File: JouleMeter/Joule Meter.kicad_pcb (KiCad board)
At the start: 4 copper layers, 153.8 x 95 mm, 82 parts, among them J1 XT60-M, J2 XT60-M, J3 22035035, J4 22035035, J5 M22-7130442, U1 LMR36510, U3 INA240A1PW, U4 ADS1118IDGS-Q1, U5 MCP6286T-E/OT1, U6 MCP2562

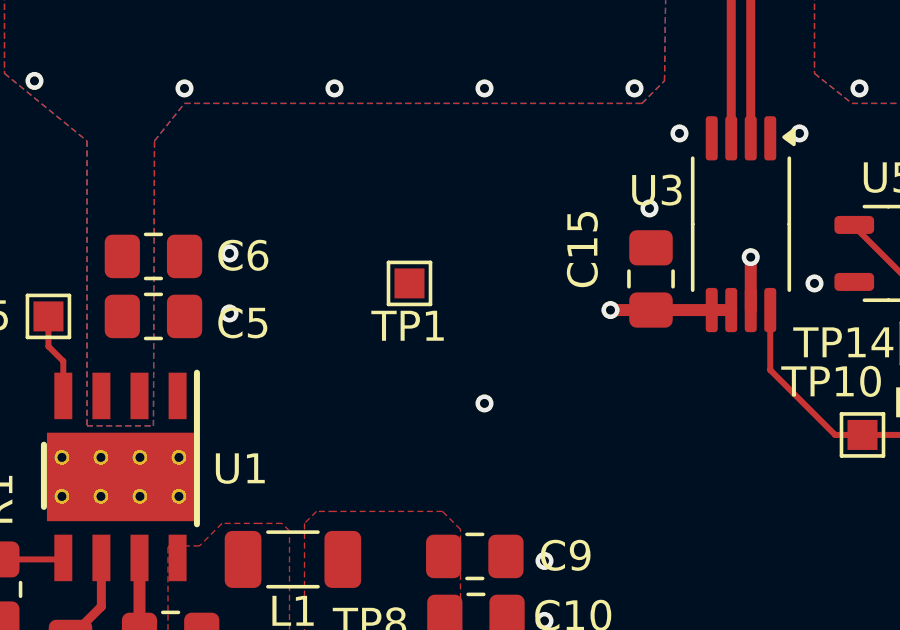
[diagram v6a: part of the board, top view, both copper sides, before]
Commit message: Joule Meter Final
Added a second test pad for the ground. The idea is that we can connect a wire across these two to make a test loop.
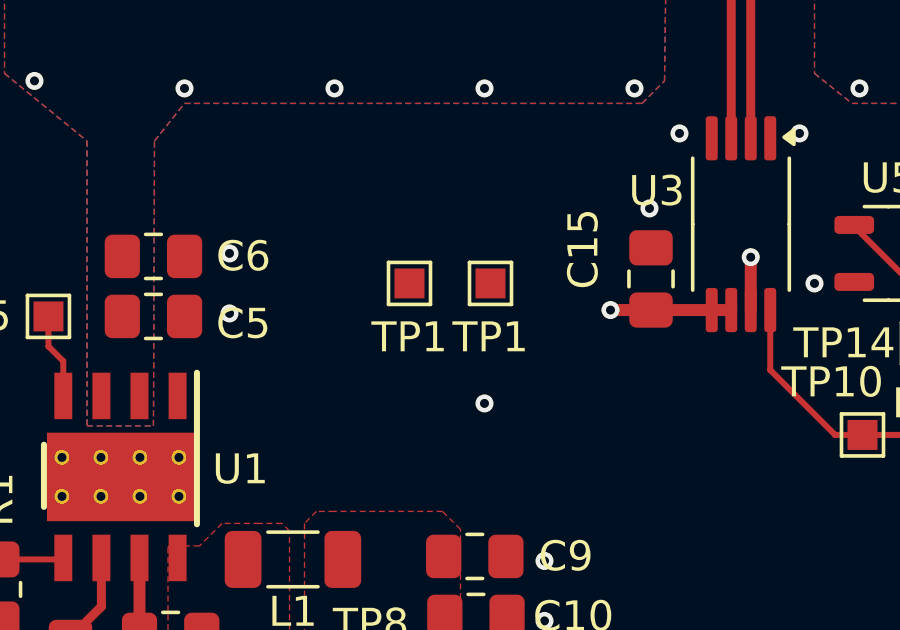
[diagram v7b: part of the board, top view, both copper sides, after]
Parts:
- added TP1: Ground, TestPoint:TestPoint_Pad_1.0x1.0mm, F.Cu at (90.2, 66.0)
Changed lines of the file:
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@@
 		(tags "test point SMD pad rectangle square")
 		(property "Reference" "TP1"
-			(at 0 -1.448 0)
+			(at 0 -1.8 0)
 			(layer "F.SilkS")
 			(effects
@@
 		)
 	)
+	(footprint "TestPoint:TestPoint_Pad_1.0x1.0mm"
+		(layer "F.Cu")
+		(at 90.2 66 180)
+		(descr "SMD rectangular pad as test Point, square 1.0mm side length")
+		(tags "test point SMD pad rectangle square")
+		(property "Reference" "TP1"
+			(at 0 -1.8 0)
+			(layer "F.SilkS")
+			(effects
+				(font
+					(size 1 1)
+					(thickness 0.15)
+				)
+			)
+		)
+		(property "Value" "Ground"
+			(at 0 1.55 0)
+			(layer "F.Fab")
+			(hide yes)
+			(effects
+				(font
+					(size 1 1)
+					(thickness 0.15)
+				)
+			)
+		)
+		(property "Datasheet" ""
+			(at 0 0 180)
+			(unlocked yes)
+			(layer "F.Fab")
+			(hide yes)
+			(effects
+				(font
+					(size 1.27 1.27)
+					(thickness 0.15)
+				)
+			)
+		)
+		(property "Description" "test point"
+			(at 0 0 180)
+			(unlocked yes)
+			(layer "F.Fab")
+			(hide yes)
+			(effects
+				(font
+					(size 1.27 1.27)
+					(thickness 0.15)
+				)
+			)
+		)
+		(attr exclude_from_pos_files)
+		(fp_line
+			(start 0.7 0.7)
+			(end -0.7 0.7)
+			(stroke
+				(width 0.12)
+				(type solid)
+			)
+			(layer "F.SilkS")
+		)
+		(fp_line
+			(start 0.7 -0.7)
+			(end 0.7 0.7)
+			(stroke
+				(width 0.12)
+				(type solid)
+			)
+			(layer "F.SilkS")
+		)
+		(fp_line
+			(start -0.7 0.7)
+			(end -0.7 -0.7)
+			(stroke
+				(width 0.12)
+				(type solid)
+			)
+			(layer "F.SilkS")
+		)
+		(fp_line
+			(start -0.7 -0.7)
+			(end 0.7 -0.7)
+			(stroke
+				(width 0.12)
+				(type solid)
+			)
+			(layer "F.SilkS")
+		)
+		(fp_line
+			(start 1 1)
+			(end 1 -1)
+			(stroke
+				(width 0.05)
+				(type solid)
+			)
+			(layer "F.CrtYd")
+		)
+		(fp_line
+			(start 1 1)
+			(end -1 1)
+			(stroke
+				(width 0.05)
+				(type solid)
+			)
+			(layer "F.CrtYd")
+		)
+		(fp_line
+			(start -1 -1)
+			(end 1 -1)
+			(stroke
+				(width 0.05)
+				(type solid)
+			)
+			(layer "F.CrtYd")
+		)
+		(fp_line
+			(start -1 -1)
+			(end -1 1)
+			(stroke
+				(width 0.05)
+				(type solid)
+			)
+			(layer "F.CrtYd")
+		)
+		(fp_text user "${REFERENCE}"
+			(at 0.05 1.7875 0)
+			(layer "F.Fab")
+			(effects
+				(font
+					(size 1 1)
+					(thickness 0.15)
+				)
+			)
+		)
+		(pad "1" smd rect
+			(at 0 0 180)
+			(size 1 1)
+			(layers "F.Cu" "F.Mask")
+			(net 1 "GND")
+			(pinfunction "1")
+			(pintype "passive")
+		)
+		(embedded_fonts no)
+	)
 	(footprint "Resistor_SMD:R_0805_2012Metric"

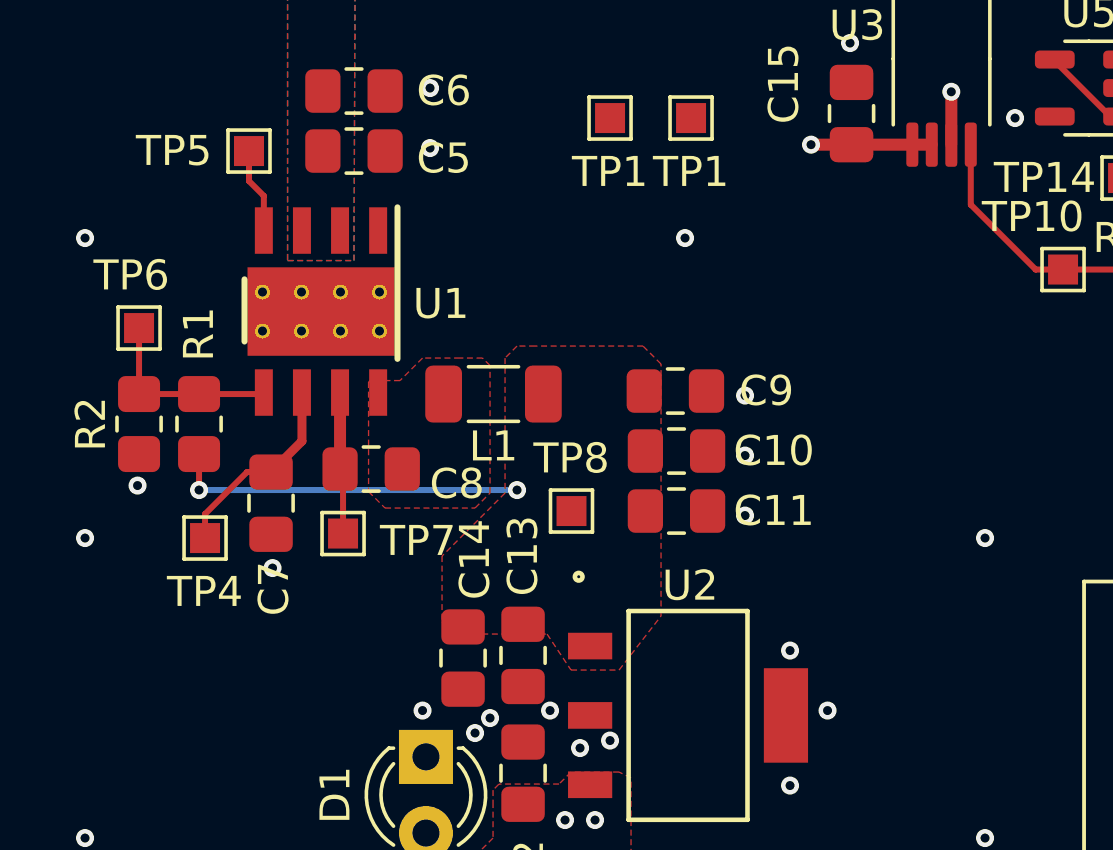
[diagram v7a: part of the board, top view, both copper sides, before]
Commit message: changed the inductor footprint
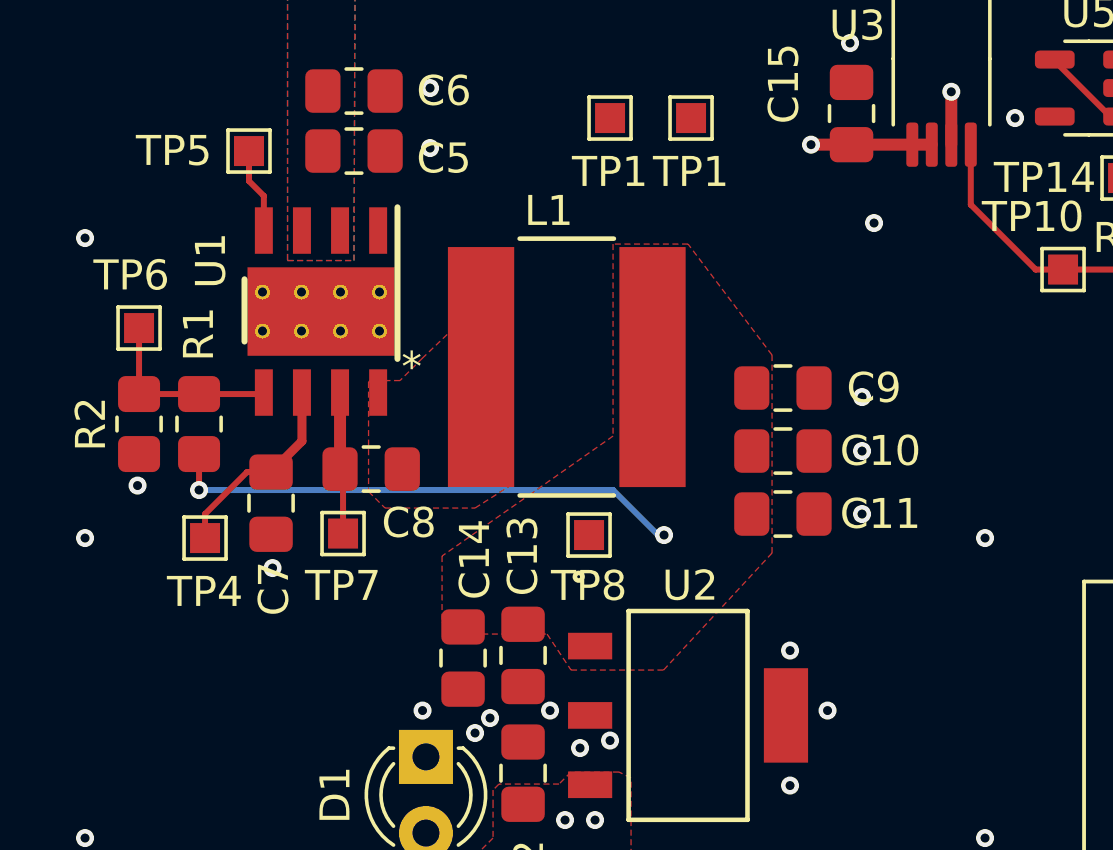
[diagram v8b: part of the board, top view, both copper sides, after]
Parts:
- L1: footprint Inductor_SMD:L_1206_3216Metric_Pad1.22x1.90mm_HandSolder -> Personal:IND_BOURNS_SRN8040
- moved C9 3.59 mm to (93.3, 75.0)
- moved C11 3.55 mm to (93.3, 79.2)
- moved C10 3.55 mm to (93.3, 77.1)
- moved L1 2.60 mm to (86.1, 74.3)
- moved TP8 0.99 mm to (86.8, 79.9)
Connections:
- C1 pad 3: GND -> (no net)
- C1 pad 4: Net-(J1-POS) -> (no net)
- C3 pad 3: Net-(J2-POS) -> (no net)
- C3 pad 4: GND -> (no net)
- R0 pad 2: Net-(J2-POS) -> Net-(J1-POS)
- U1 pad 10: GND -> (no net)
- U1 pad 11: GND -> (no net)
- U1 pad 12: GND -> (no net)
- U1 pad 13: GND -> (no net)
- U1 pad 14: GND -> (no net)
- U1 pad 15: GND -> (no net)
- U1 pad 16: GND -> (no net)
- U1 pad 17: GND -> (no net)
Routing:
- net +7V: track 11.8 -> 17.3 mm
